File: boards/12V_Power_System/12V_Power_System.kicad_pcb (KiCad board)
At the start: 2 copper layers, 3 parts, among them J1 Screw_Terminal_01x02, J2 Motor_Controller_Term_01x02

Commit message: footprints
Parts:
- added J10: Motor_Controller_5_Term_01x02, TerminalBlock:TerminalBlock_Xinya_XY308-2.54-2P_1x02_P2.54mm_Horizontal, F.Cu at (145.1, 117.5)
- added J4: Motor_Controller_2_Term_01x02, TerminalBlock:TerminalBlock_Xinya_XY308-2.54-2P_1x02_P2.54mm_Horizontal, F.Cu at (122.2, 117.5)
- added J6: Motor_Controller_1_Term_01x02, TerminalBlock:TerminalBlock_Xinya_XY308-2.54-2P_1x02_P2.54mm_Horizontal, F.Cu at (129.8, 117.5)
- added J8: Motor_Controller_4_Term_01x02, TerminalBlock:TerminalBlock_Xinya_XY308-2.54-2P_1x02_P2.54mm_Horizontal, F.Cu at (137.4, 117.5)
- added U1: irhapsody_relay_12vdc_8060a_1, REAAAL:IRhapsody Relay 12VDC 8060A, F.Cu at (143.0, 62.3)
- added U2: irhapsody_relay_12vdc_8060a_2, REAAAL:IRhapsody Relay 12VDC 8060A, F.Cu at (133.9, 98.1)
- added U3: irhapsody_relay_12vdc_8060a_3, REAAAL:IRhapsody Relay 12VDC 8060A, F.Cu at (162.4, 98.1)
- added U4: irhapsody_relay_12vdc_8060a_4, REAAAL:IRhapsody Relay 12VDC 8060A, F.Cu at (191.0, 98.1)
- added U5: irhapsody_relay_12vdc_8060a_5, REAAAL:IRhapsody Relay 12VDC 8060A, F.Cu at (219.5, 98.1)
- added ZENER_DIODE2: 16Vz, Diode_THT:D_DO-34_SOD68_P10.16mm_Horizontal, F.Cu at (151.7, 114.9)
- added ZENER_DIODE3: 16Vz, Diode_THT:D_DO-34_SOD68_P10.16mm_Horizontal, F.Cu at (151.7, 118.1)
- added ZENER_DIODE4: 16Vz, Diode_THT:D_DO-34_SOD68_P10.16mm_Horizontal, F.Cu at (151.7, 121.2)
- added ZENER_DIODE5: 16Vz, Diode_THT:D_DO-34_SOD68_P10.16mm_Horizontal, F.Cu at (151.7, 124.4)
- J2: value Motor_Controller_Term_01x02 -> Motor_Controller_1_Term_01x02
- moved ZENER_DIODE1 23.4 mm to (115.3, 61.0)
- moved J1 22.2 mm to (119.7, 70.0)
- moved J2 22.1 mm to (119.5, 52.0)
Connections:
- net MC+ renamed MC_1+

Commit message: updated schematic
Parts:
- added E-STOP5: E-STOP NC, REAAAL:E-Stop, F.Cu at (177.2, 42.2)
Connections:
- U1 pad 5: Net-(E-STOP1A-B) -> Net-(E-STOP5A-B)
- U2 pad 5: Net-(E-STOP2A-B) -> Net-(E-STOP5A-B)
- U3 pad 5: Net-(E-STOP3A-B) -> Net-(E-STOP5A-B)
- U4 pad 5: Net-(E-STOP4A-B) -> Net-(E-STOP5A-B)
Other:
- board outline added: 12.4 x 13.7 mm

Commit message: updated board layout
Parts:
- removed J10: Motor_Controller_5_Term_01x02, TerminalBlock:TerminalBlock_Xinya_XY308-2.54-2P_1x02_P2.54mm_Horizontal
- removed J8: Motor_Controller_4_Term_01x02, TerminalBlock:TerminalBlock_Xinya_XY308-2.54-2P_1x02_P2.54mm_Horizontal
- added J3: 1986660-2, REAAAL:TE_1986660-2, F.Cu at (127.8, 134.3)
- added J5: 1986660-2, REAAAL:TE_1986660-2, F.Cu at (193.8, 134.3)
- J1: value Screw_Terminal_01x02 -> 1986660-2; footprint TerminalBlock:TerminalBlock_Xinya_XY308-2.54-2P_1x02_P2.54mm_Horizontal -> REAAAL:TE_1986660-2
- J2, J6: value Motor_Controller_1_Term_01x02 -> 1986660-2; footprint TerminalBlock:TerminalBlock_Xinya_XY308-2.54-2P_1x02_P2.54mm_Horizontal -> REAAAL:TE_1986660-2
- J4: value Motor_Controller_2_Term_01x02 -> 1986660-2; footprint TerminalBlock:TerminalBlock_Xinya_XY308-2.54-2P_1x02_P2.54mm_Horizontal -> REAAAL:TE_1986660-2
- moved E-STOP5 122.3 mm to (66.0, 93.0), turned to -90 degrees
- moved J6 97.5 mm to (225.8, 134.3)
- moved J2 85.8 mm to (95.4, 134.3)
- moved ZENER_DIODE5 84.0 mm to (235.7, 122.0), turned to 180 degrees
- moved J1 76.9 mm to (63.3, 122.3)
- moved ZENER_DIODE1 64.3 mm to (95.1, 122.0)
- moved U1 58.2 mm to (97.1, 98.1)
- moved ZENER_DIODE4 51.9 mm to (203.6, 122.0), turned to 180 degrees
- moved J4 42.0 mm to (160.7, 134.3)
- moved ZENER_DIODE3 19.3 mm to (170.5, 122.0), turned to 180 degrees
- moved ZENER_DIODE2 15.7 mm to (137.6, 122.0), turned to 180 degrees
- moved U5 8.04 mm to (227.5, 98.1)
- moved U4 4.54 mm to (195.5, 98.1)
- moved U2 4.38 mm to (129.5, 98.1)
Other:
- board size 12.4 x 13.7 mm -> 13.7 x 12.4 mm

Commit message: Updated Schematic and PCB
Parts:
- moved ZENER_DIODE1 10.2 mm to (105.2, 122.0), turned to 180 degrees
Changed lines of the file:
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@@
 	(footprint "Diode_THT:D_DO-34_SOD68_P10.16mm_Horizontal"
 		(layer "F.Cu")
-		(at 95.0875 122)
+		(at 105.2475 122 180)
 		(descr "Diode, DO-34_SOD68 series, Axial, Horizontal, pin pitch=10.16mm, , length*diameter=3.04*1.6mm^2, , https://www.nxp.com/docs/en/data-sheet/KTY83_SER.pdf")
 		(tags "Diode DO-34_SOD68 series Axial Horizontal pin pitch 10.16mm  length 3.04mm diameter 1.6mm")
@@
 		)
 		(property "Footprint" "Diode_THT:D_DO-34_SOD68_P10.16mm_Horizontal"
-			(at 0 0 0)
+			(at 0 0 180)
 			(unlocked yes)
 			(layer "F.Fab")
@@
 		)
 		(property "Datasheet" ""
-			(at 0 0 0)
+			(at 0 0 180)
 			(unlocked yes)
 			(layer "F.Fab")
@@
 		)
 		(property "Description" "Zener diode, filled shape"
-			(at 0 0 0)
+			(at 0 0 180)
 			(unlocked yes)
 			(layer "F.Fab")
@@
 		(attr through_hole)
 		(fp_line
+			(start 9.17 0)
+			(end 6.72 0)
+			(stroke
+				(width 0.12)
+				(type solid)
+			)
+			(layer "F.SilkS")
+		)
+		(fp_line
+			(start 6.72 0.92)
+			(end 6.72 -0.92)
+			(stroke
+				(width 0.12)
+				(type solid)
+			)
+			(layer "F.SilkS")
+		)
+		(fp_line
+			(start 6.72 -0.92)
+			(end 3.44 -0.92)
+			(stroke
+				(width 0.12)
+				(type solid)
+			)
+			(layer "F.SilkS")
+		)
+		(fp_line
+			(start 4.136 -0.92)
+			(end 4.136 0.92)
+			(stroke
+				(width 0.12)
+				(type solid)
+			)
+			(layer "F.SilkS")
+		)
+		(fp_line
+			(start 4.016 -0.92)
+			(end 4.016 0.92)
+			(stroke
+				(width 0.12)
+				(type solid)
+			)
+			(layer "F.SilkS")
+		)
+		(fp_line
+			(start 3.896 -0.92)
+			(end 3.896 0.92)
+			(stroke
+				(width 0.12)
+				(type solid)
+			)
+			(layer "F.SilkS")
+		)
+		(fp_line
+			(start 3.44 0.92)
+			(end 6.72 0.92)
+			(stroke
+				(width 0.12)
+				(type solid)
+			)
+			(layer "F.SilkS")
+		)
+		(fp_line
+			(start 3.44 -0.92)
+			(end 3.44 0.92)
+			(stroke
+				(width 0.12)
+				(type solid)
+			)
+			(layer "F.SilkS")
+		)
+		(fp_line
 			(start 0.99 0)
 			(end 3.44 0)
@@
 		)
 		(fp_line
-			(start 3.44 -0.92)
-			(end 3.44 0.92)
-			(stroke
-				(width 0.12)
-				(type solid)
-			)
-			(layer "F.SilkS")
-		)
-		(fp_line
-			(start 3.44 0.92)
-			(end 6.72 0.92)
-			(stroke
-				(width 0.12)
-				(type solid)
-			)
-			(layer "F.SilkS")
-		)
-		(fp_line
-			(start 3.896 -0.92)
-			(end 3.896 0.92)
-			(stroke
-				(width 0.12)
-				(type solid)
-			)
-			(layer "F.SilkS")
-		)
-		(fp_line
-			(start 4.016 -0.92)
-			(end 4.016 0.92)
-			(stroke
-				(width 0.12)
-				(type solid)
-			)
-			(layer "F.SilkS")
-		)
-		(fp_line
-			(start 4.136 -0.92)
-			(end 4.136 0.92)
-			(stroke
-				(width 0.12)
-				(type solid)
-			)
-			(layer "F.SilkS")
-		)
-		(fp_line
-			(start 6.72 -0.92)
-			(end 3.44 -0.92)
-			(stroke
-				(width 0.12)
-				(type solid)
-			)
-			(layer "F.SilkS")
-		)
-		(fp_line
-			(start 6.72 0.92)
-			(end 6.72 -0.92)
-			(stroke
-				(width 0.12)
-				(type solid)
-			)
-			(layer "F.SilkS")
-		)
-		(fp_line
-			(start 9.17 0)
-			(end 6.72 0)
-			(stroke
-				(width 0.12)
-				(type solid)
-			)
-			(layer "F.SilkS")
+			(start 11.16 1.05)
+			(end 11.16 -1.05)
+			(stroke
+				(width 0.05)
+				(type solid)
+			)
+			(layer "F.CrtYd")
+		)
+		(fp_line
+			(start 11.16 -1.05)
+			(end -1 -1.05)
+			(stroke
+				(width 0.05)
+				(type solid)
+			)
+			(layer "F.CrtYd")
+		)
+		(fp_line
+			(start -1 1.05)
+			(end 11.16 1.05)
+			(stroke
+				(width 0.05)
+				(type solid)
+			)
+			(layer "F.CrtYd")
 		)
 		(fp_line
@@
 		)
 		(fp_line
-			(start -1 1.05)
-			(end 11.16 1.05)
-			(stroke
-				(width 0.05)
-				(type solid)
-			)
-			(layer "F.CrtYd")
-		)
-		(fp_line
-			(start 11.16 -1.05)
-			(end -1 -1.05)
-			(stroke
-				(width 0.05)
-				(type solid)
-			)
-			(layer "F.CrtYd")
-		)
-		(fp_line
-			(start 11.16 1.05)
-			(end 11.16 -1.05)
-			(stroke
-				(width 0.05)
-				(type solid)
-			)
-			(layer "F.CrtYd")
+			(start 10.16 0)
+			(end 6.6 0)
+			(stroke
+				(width 0.1)
+				(type solid)
+			)
+			(layer "F.Fab")
+		)
+		(fp_line
+			(start 6.6 0.8)
+			(end 6.6 -0.8)
+			(stroke
+				(width 0.1)
+				(type solid)
+			)
+			(layer "F.Fab")
+		)
+		(fp_line
+			(start 6.6 -0.8)
+			(end 3.56 -0.8)
+			(stroke
+				(width 0.1)
+				(type solid)
+			)
+			(layer "F.Fab")
+		)
+		(fp_line
+			(start 4.116 -0.8)
+			(end 4.116 0.8)
+			(stroke
+				(width 0.1)
+				(type solid)
+			)
+			(layer "F.Fab")
+		)
+		(fp_line
+			(start 4.016 -0.8)
+			(end 4.016 0.8)
+			(stroke
+				(width 0.1)
+				(type solid)
+			)
+			(layer "F.Fab")
+		)
+		(fp_line
+			(start 3.916 -0.8)
+			(end 3.916 0.8)
+			(stroke
+				(width 0.1)
+				(type solid)
+			)
+			(layer "F.Fab")
+		)
+		(fp_line
+			(start 3.56 0.8)
+			(end 6.6 0.8)
+			(stroke
+				(width 0.1)
+				(type solid)
+			)
+			(layer "F.Fab")
+		)
+		(fp_line
+			(start 3.56 -0.8)
+			(end 3.56 0.8)
+			(stroke
+				(width 0.1)
+				(type solid)
+			)
+			(layer "F.Fab")
 		)
 		(fp_line
@@
 			(layer "F.Fab")
 		)
-		(fp_line
-			(start 3.56 -0.8)
-			(end 3.56 0.8)
-			(stroke
-				(width 0.1)
-				(type solid)
-			)
-			(layer "F.Fab")
-		)
-		(fp_line
-			(start 3.56 0.8)
-			(end 6.6 0.8)
-			(stroke
-				(width 0.1)
-				(type solid)
-			)
-			(layer "F.Fab")
-		)
-		(fp_line
-			(start 3.916 -0.8)
-			(end 3.916 0.8)
-			(stroke
-				(width 0.1)
-				(type solid)
-			)
-			(layer "F.Fab")
-		)
-		(fp_line
-			(start 4.016 -0.8)
-			(end 4.016 0.8)
-			(stroke
-				(width 0.1)
-				(type solid)
-			)
-			(layer "F.Fab")
-		)
-		(fp_line
-			(start 4.116 -0.8)
-			(end 4.116 0.8)
-			(stroke
-				(width 0.1)
-				(type solid)
-			)
-			(layer "F.Fab")
-		)
-		(fp_line
-			(start 6.6 -0.8)
-			(end 3.56 -0.8)
-			(stroke
-				(width 0.1)
-				(type solid)
-			)
-			(layer "F.Fab")
-		)
-		(fp_line
-			(start 6.6 0.8)
-			(end 6.6 -0.8)
-			(stroke
-				(width 0.1)
-				(type solid)
-			)
-			(layer "F.Fab")
-		)
-		(fp_line
-			(start 10.16 0)
-			(end 6.6 0)
-			(stroke
-				(width 0.1)
-				(type solid)
-			)
-			(layer "F.Fab")
-		)
 		(fp_text user "K"
 			(at 0 -1.75 360)
@@
 		)
 		(pad "1" thru_hole rect
-			(at 0 0)
+			(at 0 0 180)
 			(size 1.5 1.5)
 			(drill 0.75)
@@
 		)
 		(pad "2" thru_hole oval
-			(at 10.16 0)
+			(at 10.16 0 180)
 			(size 1.5 1.5)
 			(drill 0.75)

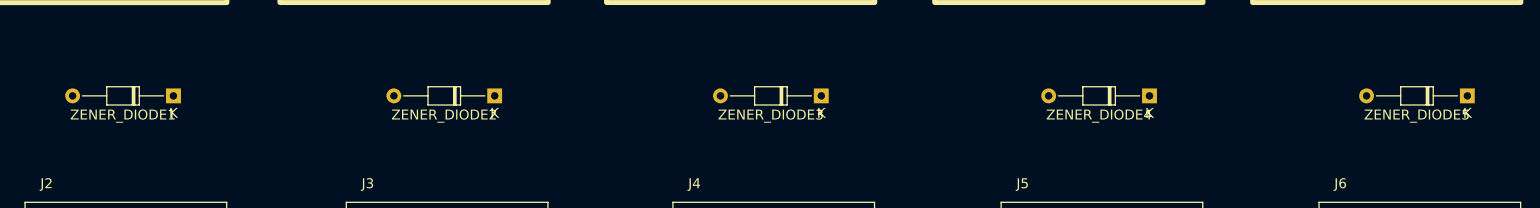
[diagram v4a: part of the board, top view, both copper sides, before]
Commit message: tidied up the schematic
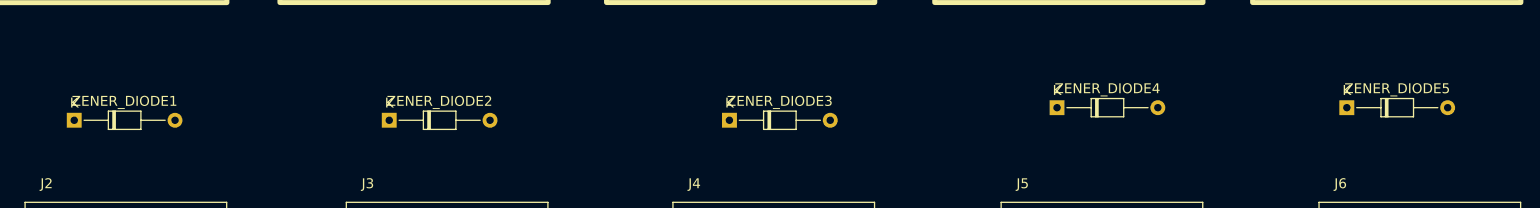
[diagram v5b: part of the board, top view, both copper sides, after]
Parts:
- moved ZENER_DIODE5 12.2 mm to (223.5, 123.2), turned to 0 degrees
- moved ZENER_DIODE2 10.9 mm to (127.0, 124.5), turned to 0 degrees
- moved ZENER_DIODE1 10.3 mm to (95.2, 124.5), turned to 0 degrees
- moved ZENER_DIODE3 9.58 mm to (161.3, 124.5), turned to 0 degrees
- moved ZENER_DIODE4 9.39 mm to (194.3, 123.2), turned to 0 degrees
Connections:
- net MC_1+ renamed Net-(J2-1)
- E-STOP5 pad 2: Net-(E-STOP5A-B) -> ESO
- U1 pad 5: Net-(E-STOP5A-B) -> ESO
- ZENER_DIODE2 pad 1: MC_2+ -> Net-(J3-1)
- ZENER_DIODE3 pad 1: MC_3+ -> Net-(J4-1)
- ZENER_DIODE4 pad 1: MC_4+ -> Net-(J5-1)
- ZENER_DIODE5 pad 1: MC_5+ -> Net-(J6-1)
